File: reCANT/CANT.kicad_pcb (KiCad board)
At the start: 4 copper layers, 82 x 49.1 mm, 74 parts, among them J1 USB_C_Receptacle_USB2.0, J2 Conn_02x08_Odd_Even, J3 Screw_Terminal_01x04, J4 Screw_Terminal_01x02, P1 SWD, SW1 SW_SPST, U1 USB3343, U10 DSC1001, U2 LD1117S33TR, U3 STM32H743VITx, U4 MCP2558FD-xSN, U5 MCP2558FD-xSN, U6 74LVC1G66, U7 74LVC1G66, U8 SN74LVC1G14DBV, U9 ST485EBDR

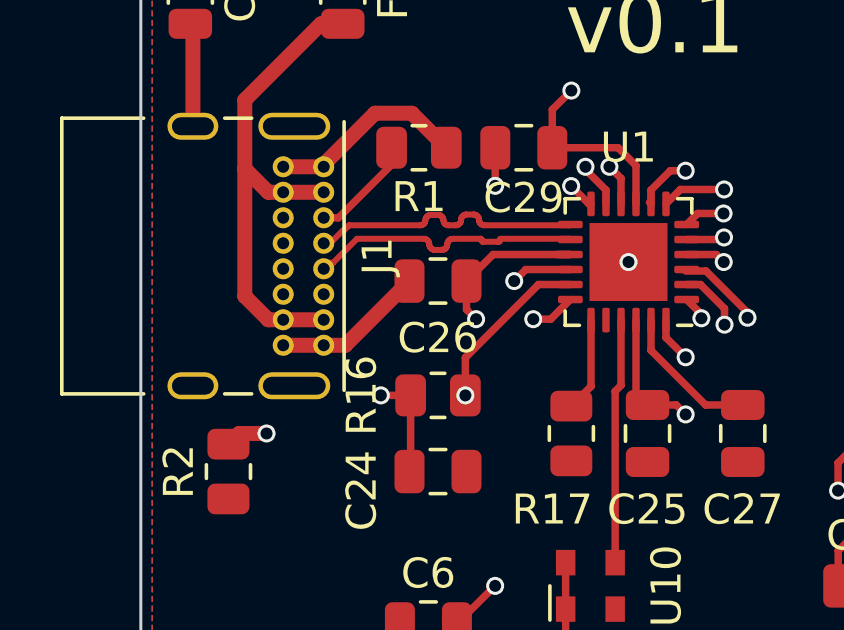
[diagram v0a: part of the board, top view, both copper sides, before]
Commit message: Fixed USB differential pair routing to have correct impedence
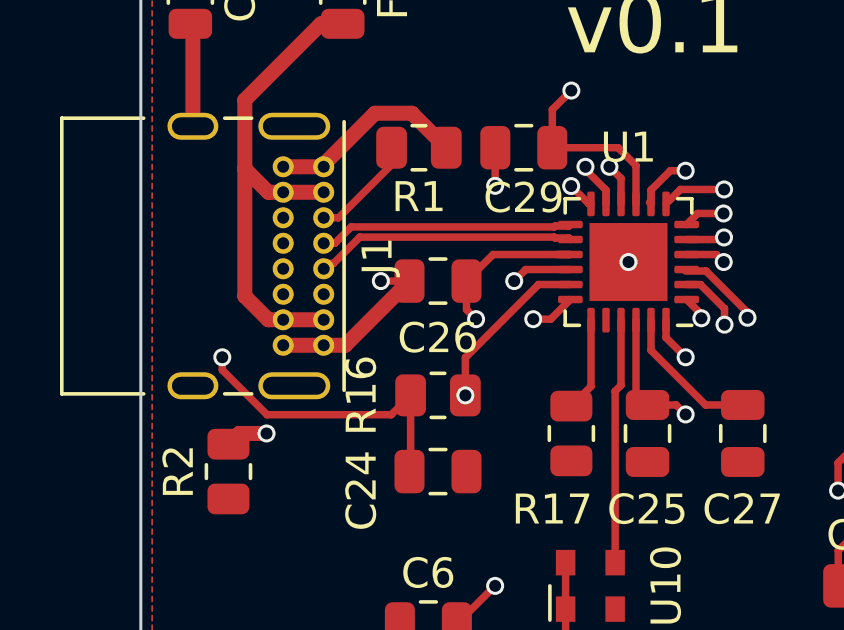
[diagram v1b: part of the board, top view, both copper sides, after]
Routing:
- net VBUS: track 105.4 -> 112.9 mm
- net GND: track 131.2 -> 132.2 mm, vias 2 -> 3
- net /HS_USB/D+: track 11.0 -> 10.4 mm
- added copper zone on In1.Cu, net GND
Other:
- net class USB Data added: clearance 0.2, trace_width 0.25, via_dia 0.6, via_drill 0.4
- rule trace_min: 0.2 -> 0.0889
- rule via_min_drill: 0.3 -> 0.2
